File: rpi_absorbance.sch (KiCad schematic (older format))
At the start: 32 parts, among them CON1 BARREL_JACK, P3 RPI_HEADER, P4 STEPPER_CONN, U1 R-78B5.0-1.5L, U3 DRV8825, U4 TCA9406DCUR

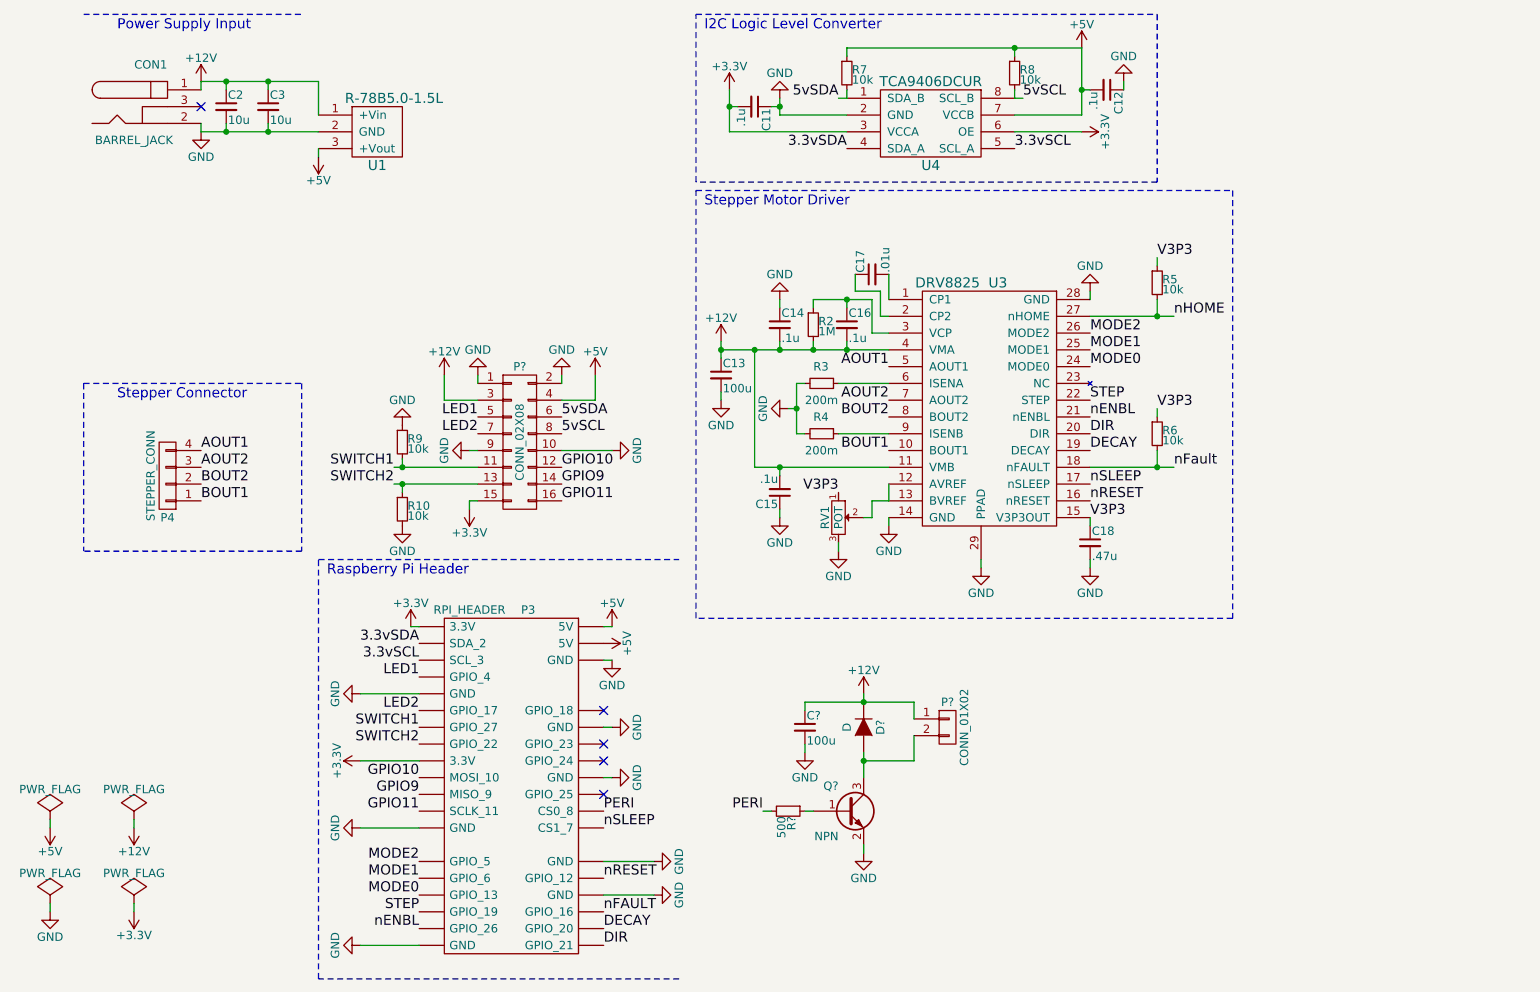
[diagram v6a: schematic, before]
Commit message: Add transistors
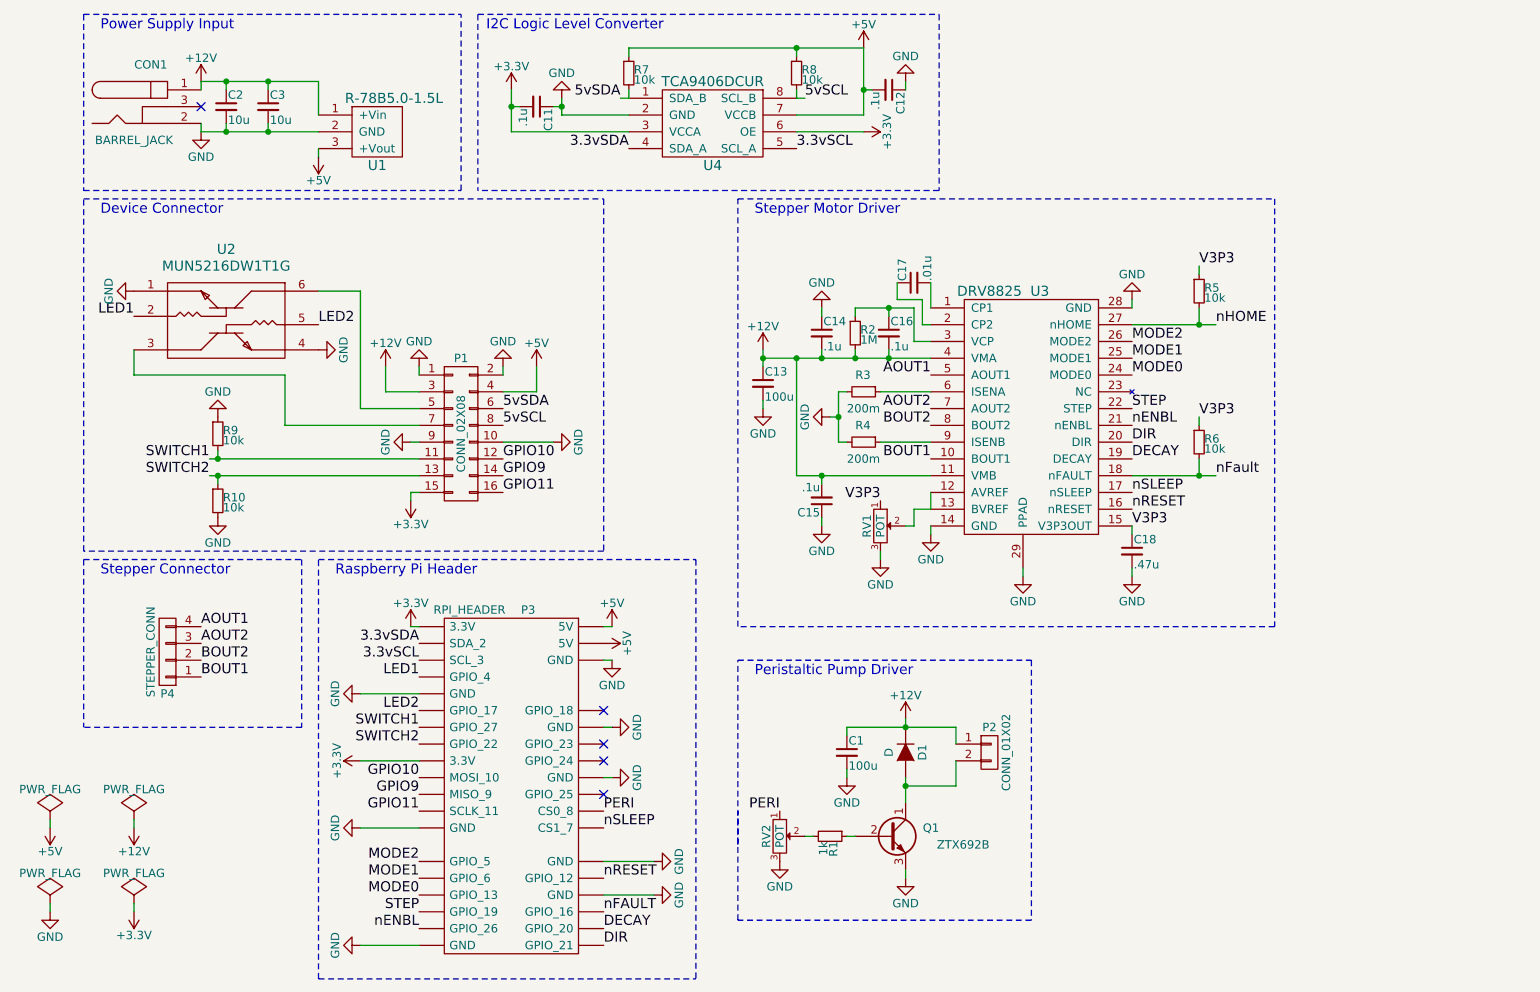
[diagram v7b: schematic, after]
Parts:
- removed Q?: NPN, footprints:3-CP, symbol Q_NPN_BEC
- added Q1: ZTX692B, symbol Q_NPN_CBE
- added RV2: POT, footprints:BOURNS_3362P, symbol POT
- added U2: MUN5216DW1T1G, symbol MUN5216DW1T1G
- C1: renamed from C?; footprint (none) -> Capacitors_ThroughHole:C_Rect_L4_W2.5_P2.5
- C13: footprint Capacitors_SMD:C_1206 -> Capacitors_ThroughHole:C_Rect_L4_W2.5_P2.5
- D1: renamed from D?; footprint (none) -> Diodes_ThroughHole:Diode_DO-41_SOD81_Horizontal_RM10
- P1: renamed from P?; footprint (none) -> Pin_Headers:Pin_Header_Straight_2x08
- P2: renamed from P?; footprint (none) -> Pin_Headers:Pin_Header_Straight_1x02
- R1: renamed from R?; value 500 -> 1k; footprint (none) -> Resistors_SMD:R_0603
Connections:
- net GND: now also Q1.3 (E), RV2.3, U2.1, U2.4
- net LED1: now also U2.2; no longer P1.5 (P5)
- net LED2: now also U2.5; no longer P1.7 (P7)
- net PERI: now also RV2.1; no longer R1.2
- net at R1.1: now also Q1.2 (B)
- net at D1.2 (A), P2.2 (P2): now also Q1.1 (C)
- new net: R1.2, RV2.2
- new net: P1.5 (P5), U2.6
- new net: P1.7 (P7), U2.3
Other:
- note added: "Device Connector"
- note added: "Peristaltic Pump Driver"
- moved on the sheet: C1, C11, C12, C13, C14, C15, C16, C17, C18, D1, P1, P2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

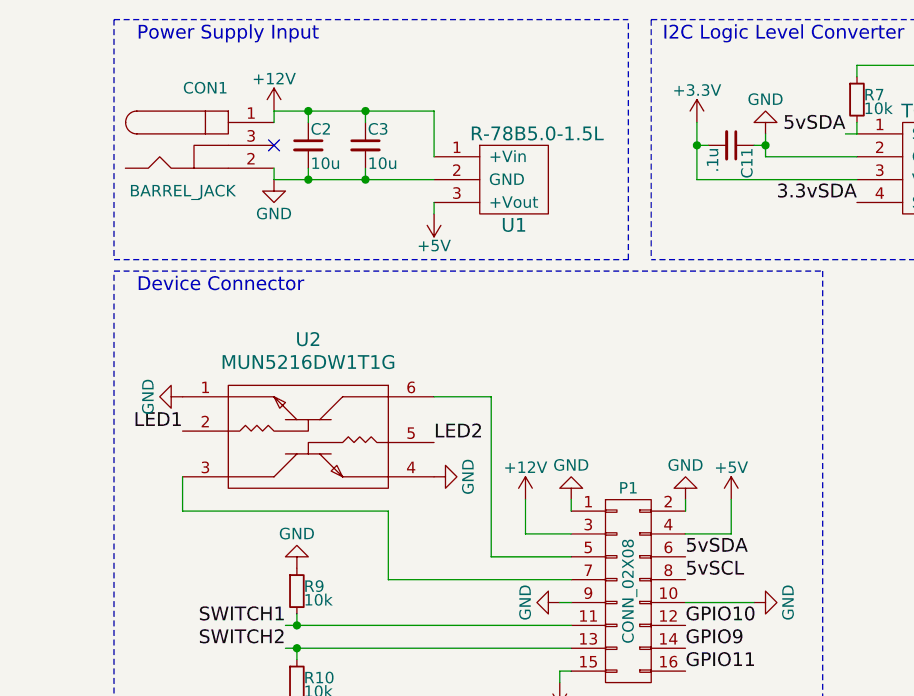
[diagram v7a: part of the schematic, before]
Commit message: Update footprints
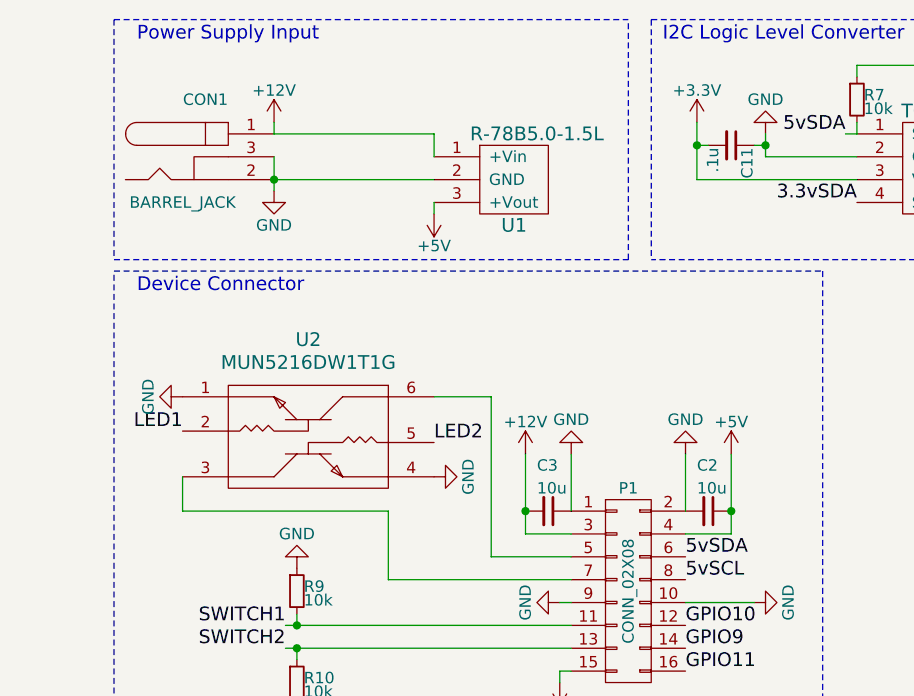
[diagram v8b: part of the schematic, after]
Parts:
- D1: footprint Diodes_ThroughHole:Diode_DO-41_SOD81_Horizontal_RM10 -> footprints:SOD-123
- Q1: footprint (none) -> TO_SOT_Packages_THT:TO-92_Inline_Narrow_Oval
- U2: footprint (none) -> footprints:SOT−363
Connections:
- net +12V: now also C3.2; no longer C2.1, C3.1
- net +5V: now also C2.1
- net GND: now also C3.1, CON1.3; no longer C3.2
- no-connect marks 5 -> 4
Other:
- moved on the sheet: C2, C3, CON1
